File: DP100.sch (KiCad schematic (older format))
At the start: 0 parts

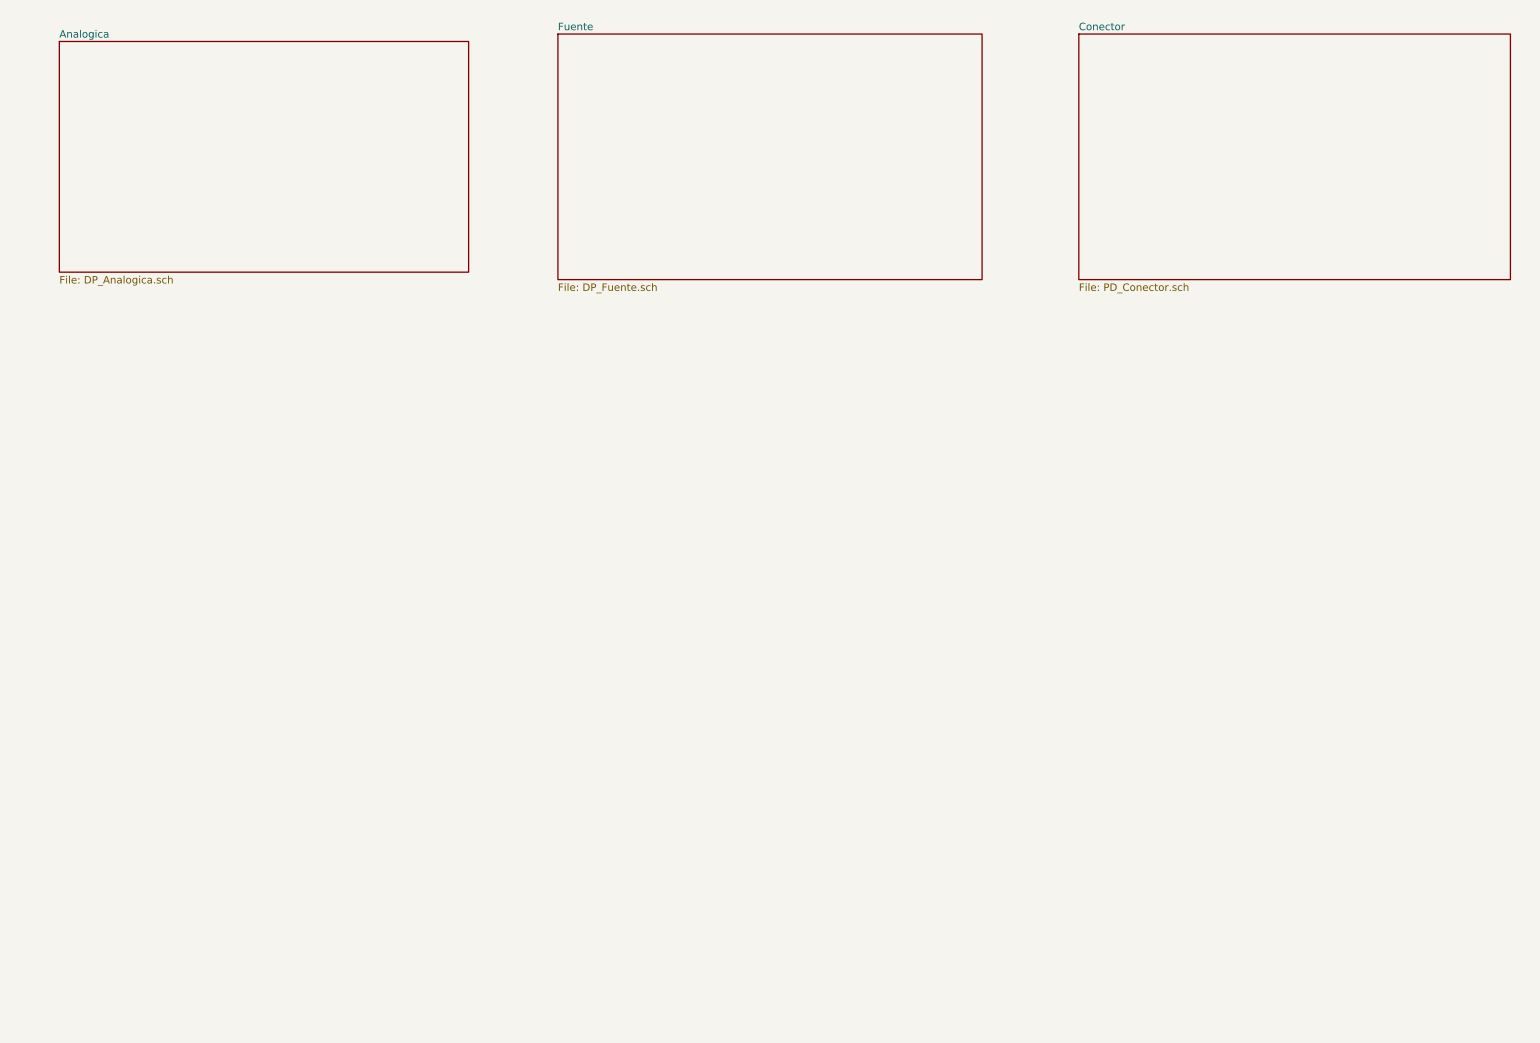
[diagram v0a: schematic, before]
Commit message: Correcciones realizadas sobre el esquematico a partir de la revision realizada el dia 2/4 por Francisco Timez
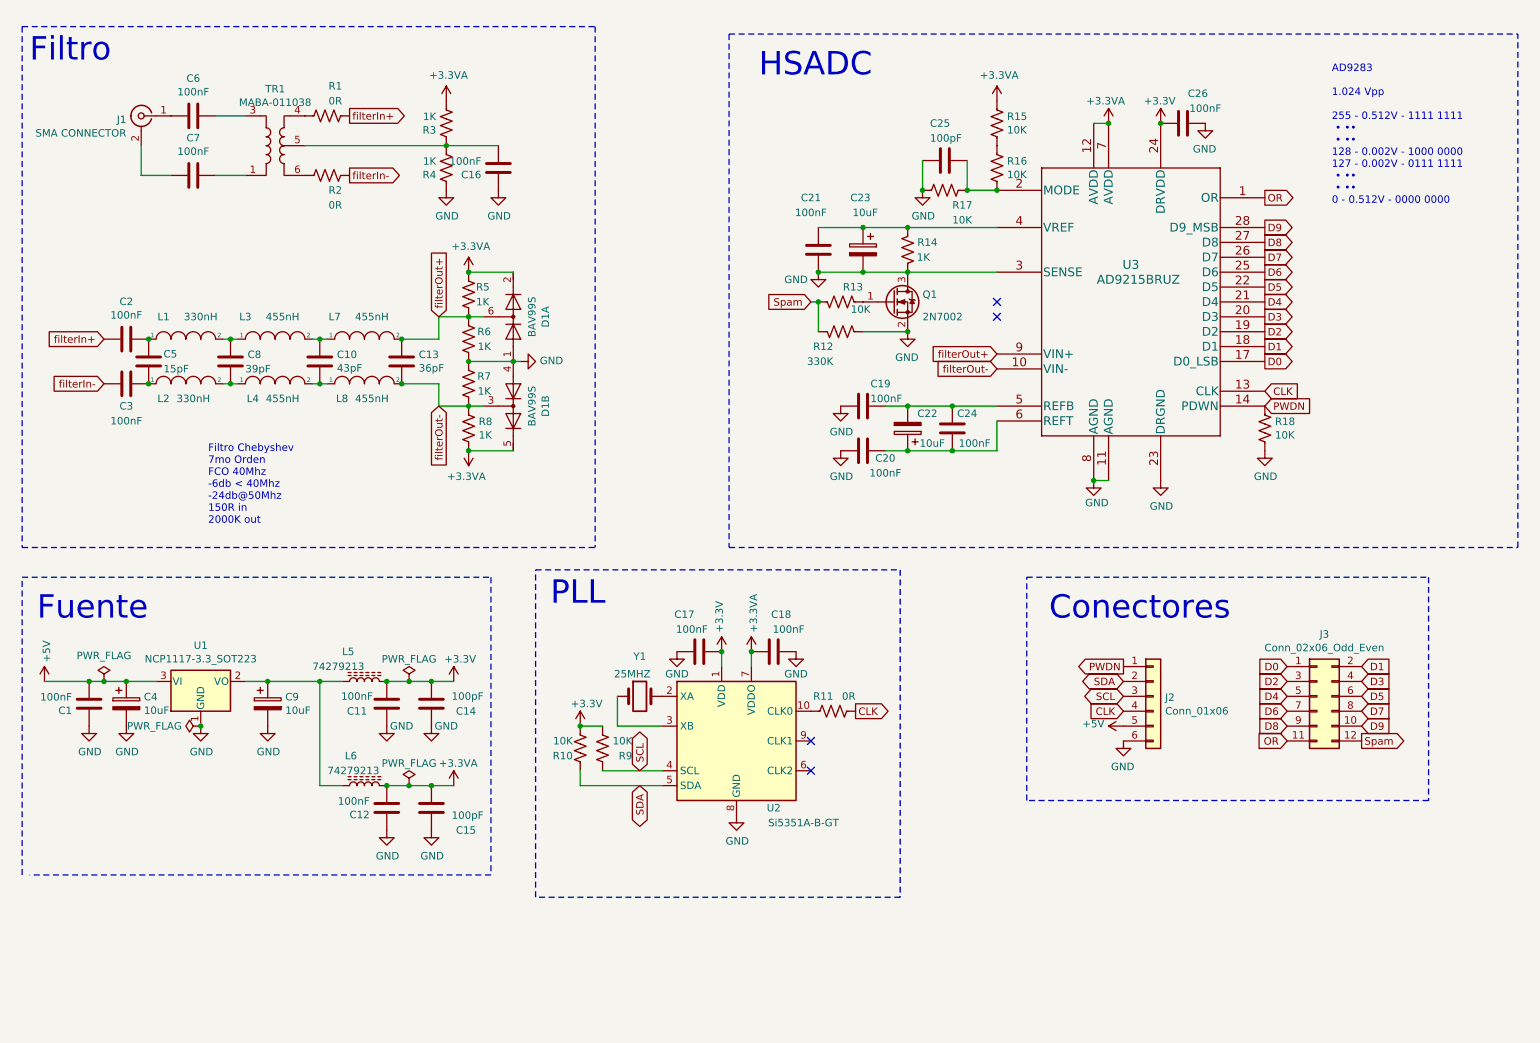
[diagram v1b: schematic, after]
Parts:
- added C1, C11, C12, C16, C17, C18, C19, C2, C20, C21, C24, C26, C3, C6, C7: 100nF, Capacitor_SMD:C_0603_1608Metric_Pad1.05x0.95mm_HandSolder, symbol Device:C
- added C10: 43pF, Capacitor_SMD:C_0603_1608Metric_Pad1.05x0.95mm_HandSolder, symbol Device:C
- added C13: 36pF, Capacitor_SMD:C_0603_1608Metric_Pad1.05x0.95mm_HandSolder, symbol Device:C
- added C14, C15, C25: 100pF, Capacitor_SMD:C_0603_1608Metric_Pad1.05x0.95mm_HandSolder, symbol Device:C
- added C22, C23, C4, C9: 10uF, Capacitor_Tantalum_SMD:CP_EIA-2012-15_AVX-P_Pad1.30x1.05mm_HandSolder, symbol Device:CP
- added C5: 15pF, Capacitor_SMD:C_0603_1608Metric_Pad1.05x0.95mm_HandSolder, symbol Device:C
- added C8: 39pF, Capacitor_SMD:C_0603_1608Metric_Pad1.05x0.95mm_HandSolder, symbol Device:C
- added D1: BAV99S, Package_TO_SOT_SMD:SOT-363_SC-70-6, symbol Diode:BAV99S
- added J1: SMA CONNECTOR, Connector_Coaxial:SMA_Amphenol_901-144_Vertical, symbol Connector:Conn_Coaxial
- added J2: Conn_01x06, Connector_PinHeader_2.54mm:PinHeader_1x06_P2.54mm_Vertical, symbol Connector_Generic:Conn_01x06
- added J3: Conn_02x06_Odd_Even, Connector_PinHeader_2.54mm:PinHeader_2x06_P2.54mm_Vertical, symbol Connector_Generic:Conn_02x06_Odd_Even
- added L1, L2: 330nH, Inductor_SMD:L_1206_3216Metric_Pad1.42x1.75mm_HandSolder, symbol pspice:INDUCTOR
- added L3, L4, L7, L8: 455nH, Inductor_SMD:L_0805_2012Metric_Pad1.15x1.40mm_HandSolder, symbol pspice:INDUCTOR
- added L5, L6: 74279213, Capacitor_SMD:C_1206_3216Metric_Pad1.42x1.75mm_HandSolder, symbol Device:L_Core_Ferrite
- added Q1: 2N7002, Package_TO_SOT_SMD:SOT-23, symbol Transistor_FET:2N7002
- added R1, R11, R2: 0R, Resistor_SMD:R_0603_1608Metric_Pad1.05x0.95mm_HandSolder, symbol Device:R_US
- added R10, R13, R15, R16, R17, R18, R9: 10K, Resistor_SMD:R_0603_1608Metric_Pad1.05x0.95mm_HandSolder, symbol Device:R_US
- added R12: 330K, Resistor_SMD:R_0603_1608Metric_Pad1.05x0.95mm_HandSolder, symbol Device:R_US
- added R14, R3, R4, R5, R6, R7, R8: 1K, Resistor_SMD:R_0603_1608Metric_Pad1.05x0.95mm_HandSolder, symbol Device:R_US
- added TR1: MABA-011038, RF_Mini-Circuits:Mini-Circuits_DB1627, symbol Transformer:ADT1-1WT
- added U1: NCP1117-3.3_SOT223, Package_TO_SOT_SMD:SOT-223-3_TabPin2, symbol Regulator_Linear:NCP1117-3.3_SOT223
- added U2: Si5351A-B-GT, Package_SO:MSOP-10_3x3mm_P0.5mm, symbol Oscillator:Si5351A-B-GT
- added U3: AD9215BRUZ, Package_SO:TSSOP-28_4.4x9.7mm_P0.65mm, symbol AD9215BRUZ:AD9215BRUZ
- added Y1: 25MHZ, Crystal:Crystal_SMD_ECS_CSM3X-2Pin_7.6x4.1mm, symbol Device:Crystal
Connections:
- new net: C9.1, L5.2, L6.1, U1.2 (VO)
- new net: C19.1, C22.2, C24.1, U3.5 (REFB)
- new net: C20.1, C22.1, C24.2, U3.6 (REFT)
- new net: C25.1, R16.2, R17.1, U3.2 (MODE)
- new net: C21.1, C23.1, R14.1, U3.4 (VREF)
- new net: R15.2, R16.1
- new net: Q1.1 (G), R13.2
- new net: R11.1, U2.10 (CLK0)
- new net: U2.2 (XA), Y1.2
- new net: U2.3 (XB), Y1.1
- new net: C16.2, R3.1, R4.2, TR1.5
- new net: C10.2, L4.2, L8.1
- new net: C10.1, L3.2, L7.1
- new net: C8.2, L2.2, L4.1
- new net: C8.1, L1.2, L3.1
- new net: C3.1, C5.2, L2.1
- new net: C2.1, C5.1, L1.1
- new net: C7.1, TR1.1
- new net: C7.2, J1.2 (Ext)
- new net: C6.1, TR1.3
- new net: C6.2, J1.1 (In)
- new net: R1.1, TR1.4
- new net: R2.1, TR1.6
- new net +3.3VA: C12.2, C15.2, C18.1, D1.2 (K2), D1.5 (K4), L6.2, R15.1, R3.2, R5.1, R8.2, U2.7 (VDDO), U3.12 (AVDD), U3.7 (AVDD)
- new net +3V3: C11.1, C14.2, C17.1, C26.2, L5.1, R10.2, R9.2, U2.1 (VDD), U3.24 (DRVDD)
- new net +5V: C1.2, C4.1, J2.5 (Pin_5), U1.3 (VI)
- new net CLK: J2.4 (Pin_4), R11.2, U3.13 (CLK)
- new net D0: J3.1 (Pin_1), U3.17 (D0_LSB)
- new net D1: J3.2 (Pin_2), U3.18 (D1)
- new net D2: J3.3 (Pin_3), U3.19 (D2)
- new net D3: J3.4 (Pin_4), U3.20 (D3)
- new net D4: J3.5 (Pin_5), U3.21 (D4)
- new net D5: J3.6 (Pin_6), U3.22 (D5)
- new net D6: J3.7 (Pin_7), U3.25 (D6)
- new net D7: J3.8 (Pin_8), U3.26 (D7)
- new net D8: J3.9 (Pin_9), U3.27 (D8)
- new net D9: J3.10 (Pin_10), U3.28 (D9_MSB)
- new net GND: C1.1, C11.2, C12.1, C14.1, C15.1, C16.1, C17.2, C18.2, C19.2, C20.2, C21.2, C23.2, C25.2, C26.1, C4.2, C9.2, D1.1 (A1), D1.4 (A3), J2.6 (Pin_6), Q1.2 (S), Q1.3 (D), R12.2, R14.2, R17.2, R18.2, R4.1, R6.1, R7.2, U1.1 (GND), U2.8 (GND), U3.11 (AGND), U3.23 (DRGND), U3.3 (SENSE), U3.8 (AGND)
- new net OR: J3.11 (Pin_11), U3.1 (OR)
- new net PWDN: J2.1 (Pin_1), R18.1, U3.14 (PDWN)
- new net SCL: J2.3 (Pin_3), R9.1, U2.4 (SCL)
- new net SDA: J2.2 (Pin_2), R10.1, U2.5 (SDA)
- new net Spam: J3.12 (Pin_12), R12.1, R13.1
- new net filterIn+: C2.2, R1.2
- new net filterIn-: C3.2, R2.2
- new net filterOut+: C13.1, D1.6 (K3A4), L7.2, R5.2, R6.2, U3.9 (VIN+)
- new net filterOut-: C13.2, D1.3 (K1A2), L8.2, R7.1, R8.1, U3.10 (VIN-)
- no-connect marks 0 -> 4
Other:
- note added: "AD9283\n\n1.024 Vpp\n\n255 - 0.512V - 1111 1111\n • ••\n • ••\n128 - 0.002V - 1000 0000\n127 - 0.002V - 0111 1111\n • ••\n • ••\n0 - 0.512V - 0000 0000"
- note added: "Conectores"
- note added: "Filtro"
- note added: "Filtro Chebyshev\n7mo Orden\nFCO 40Mhz\n-6db < 40Mhz\n-24db@50Mhz\n150R in \n2000K out"
- note added: "Fuente"
- note added: "HSADC"
- note added: "PLL"

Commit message: Cambio de etiquetas globales por jerarquicas en el esquematico. Posicionamiento de componentes y ruteo de PCB
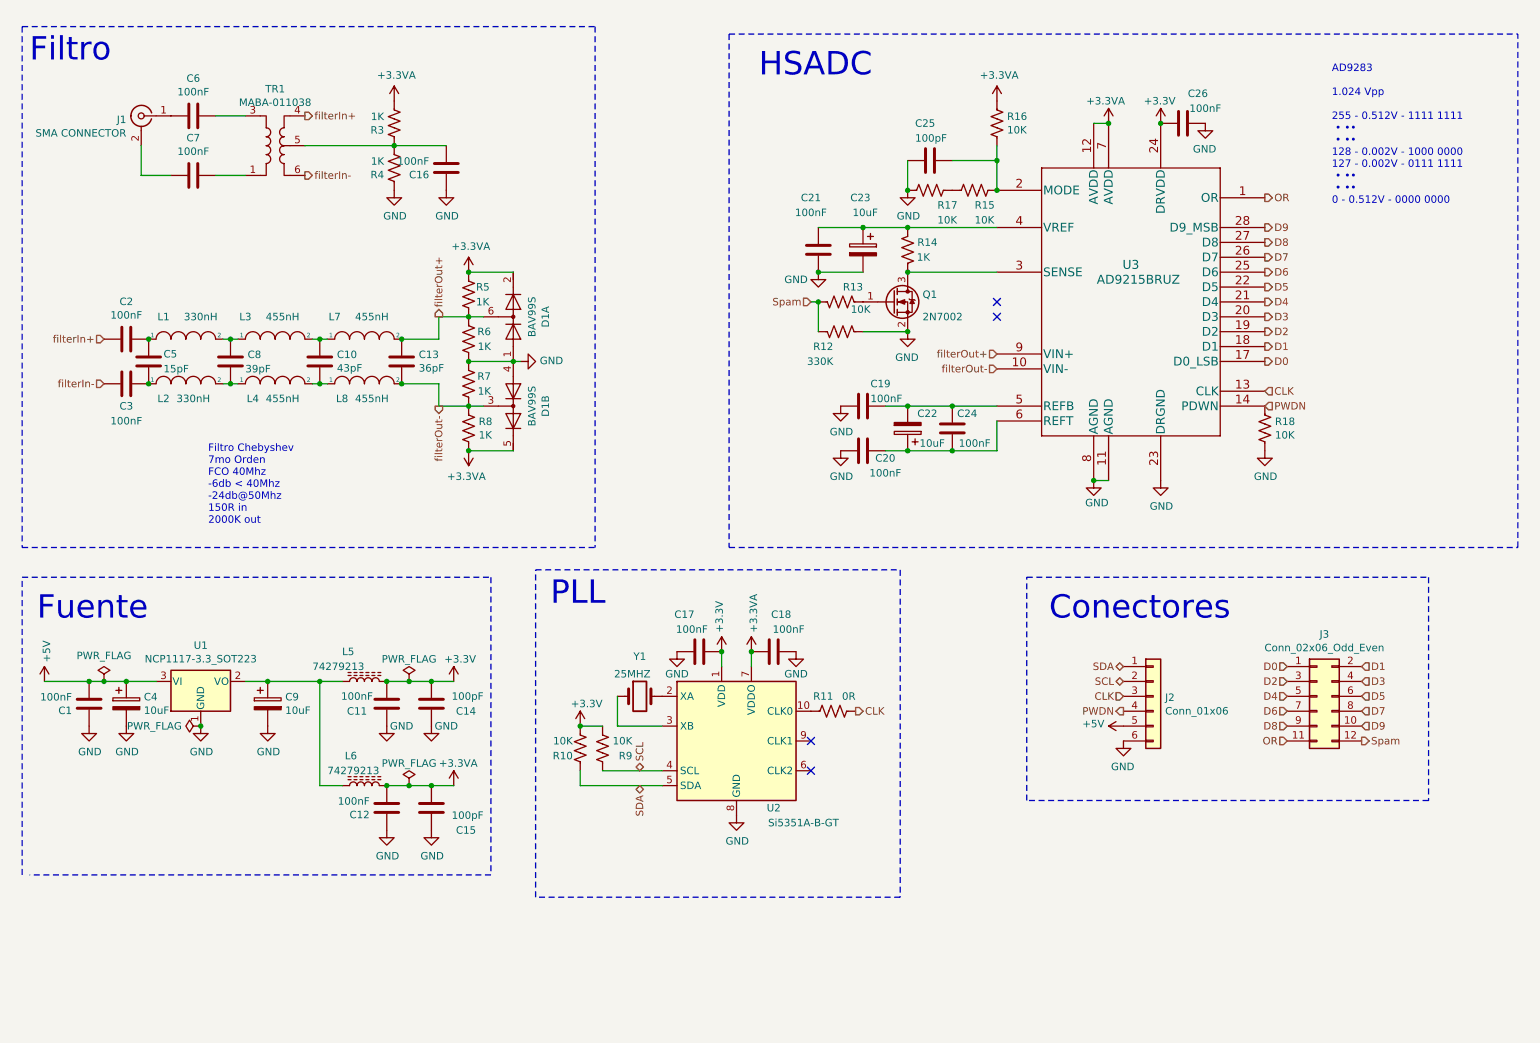
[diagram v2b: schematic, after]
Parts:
- removed R1, R2: 0R, Resistor_SMD:R_0603_1608Metric_Pad1.05x0.95mm_HandSolder, symbol Device:R_US
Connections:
- net +3.3VA: now also R16.1; no longer R15.1
- net CLK: now also J2.3 (Pin_3); no longer J2.4 (Pin_4)
- net GND: no longer Q1.3 (D), R14.2, U3.3 (SENSE)
- net PWDN: now also J2.4 (Pin_4); no longer J2.1 (Pin_1)
- net SCL: now also J2.2 (Pin_2); no longer J2.3 (Pin_3)
- net SDA: now also J2.1 (Pin_1); no longer J2.2 (Pin_2)
- net filterIn+: now also TR1.4
- net filterIn-: now also TR1.6
- net at C25.1, R16.2, U3.2 (MODE): now also R15.1; no longer R17.1
- net at R15.2: now also R17.1; no longer R16.1
- new net: Q1.3 (D), R14.2, U3.3 (SENSE)
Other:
- moved on the sheet: C16, C25, R15, R16, R17, R3, R4
